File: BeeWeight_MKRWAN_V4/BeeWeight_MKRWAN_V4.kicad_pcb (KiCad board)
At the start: 2 copper layers, 38.2 x 67.4 mm, 31 parts, among them J10 694103107102, J2 691412120004B, J3 691412120004B, J4 691412120004B, J5 691412120004B, J7 Conn_01x14_Female, J8 Conn_01x14_Female, J9 694108301002, Q1 IRLML6244, U1 ADS1241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

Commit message: Lundi soir : en cours de pin mapping
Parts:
- added J1: SSW-120-01-X-S, SAMTEC_SSW-120-01-X-S, F.Cu at (153.6, 81.7)
- added J6: SSW-120-01-X-S, SSW-120-01-X-S:SAMTEC_SSW-120-01-X-S, F.Cu at (244.9, 84.2)
- added U3: LDL1117S33R, SOT230P700X180-4N, F.Cu at (206.4, 61.7)
- moved J7 86.4 mm to (67.5, 65.6)
- moved J8 86.4 mm to (87.8, 98.6)
- moved J9 32.5 mm to (163.6, 25.7)
- moved J10 30.8 mm to (145.3, 29.2)
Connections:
- net Net-(U2-Pad3) renamed /IO42_ALERT
- net Net-(U2-Pad6) renamed /IO42_SHT_RST
- Q1 pad 1: /D3_CMD_MOS -> /IO42_CMD_MOS
- R1 pad 2: /D3_CMD_MOS -> /IO42_CMD_MOS
- R6 pad 1: /D12_SCL -> /IO42_SCL
- R7 pad 1: /D11_SDA -> /IO42_SDA
- U1 pad 23: /D7_CS -> /IO42_CS
- U1 pad 24: /D8_MOSI -> /IO42_MOSI
- U1 pad 25: /D10_MISO -> /IO42_MISO
- U1 pad 26: /D9_SCLK -> /IO42_SCLK
- U2 pad 1: /D11_SDA -> /IO42_SDA
- U2 pad 4: /D12_SCL -> /IO42_SCL
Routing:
- net /IO42_SCL: track 0.00 -> 44.0 mm, vias 0 -> 1
- net /D12_SCL: track 44.0 -> 0.00 mm, vias 1 -> 0
- net /IO42_SDA: track 0.00 -> 38.1 mm, vias 0 -> 2
- net /D11_SDA: track 38.1 -> 0.00 mm, vias 2 -> 0
- net /IO42_CMD_MOS: track 0.00 -> 15.7 mm
- net /D3_CMD_MOS: track 15.7 -> 0.00 mm
- net /IO42_CS: track 0.00 -> 14.4 mm
- net /D7_CS: track 14.4 -> 0.00 mm
- net /IO42_MOSI: track 0.00 -> 13.9 mm
- net /D8_MOSI: track 13.9 -> 0.00 mm
- net /IO42_SCLK: track 0.00 -> 11.2 mm
- net /D9_SCLK: track 11.2 -> 0.00 mm
- net /IO42_MISO: track 0.00 -> 10.6 mm, vias 0 -> 1
- net /D10_MISO: track 10.6 -> 0.00 mm, vias 1 -> 0
- net /Vin: track 27.1 -> 18.8 mm
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
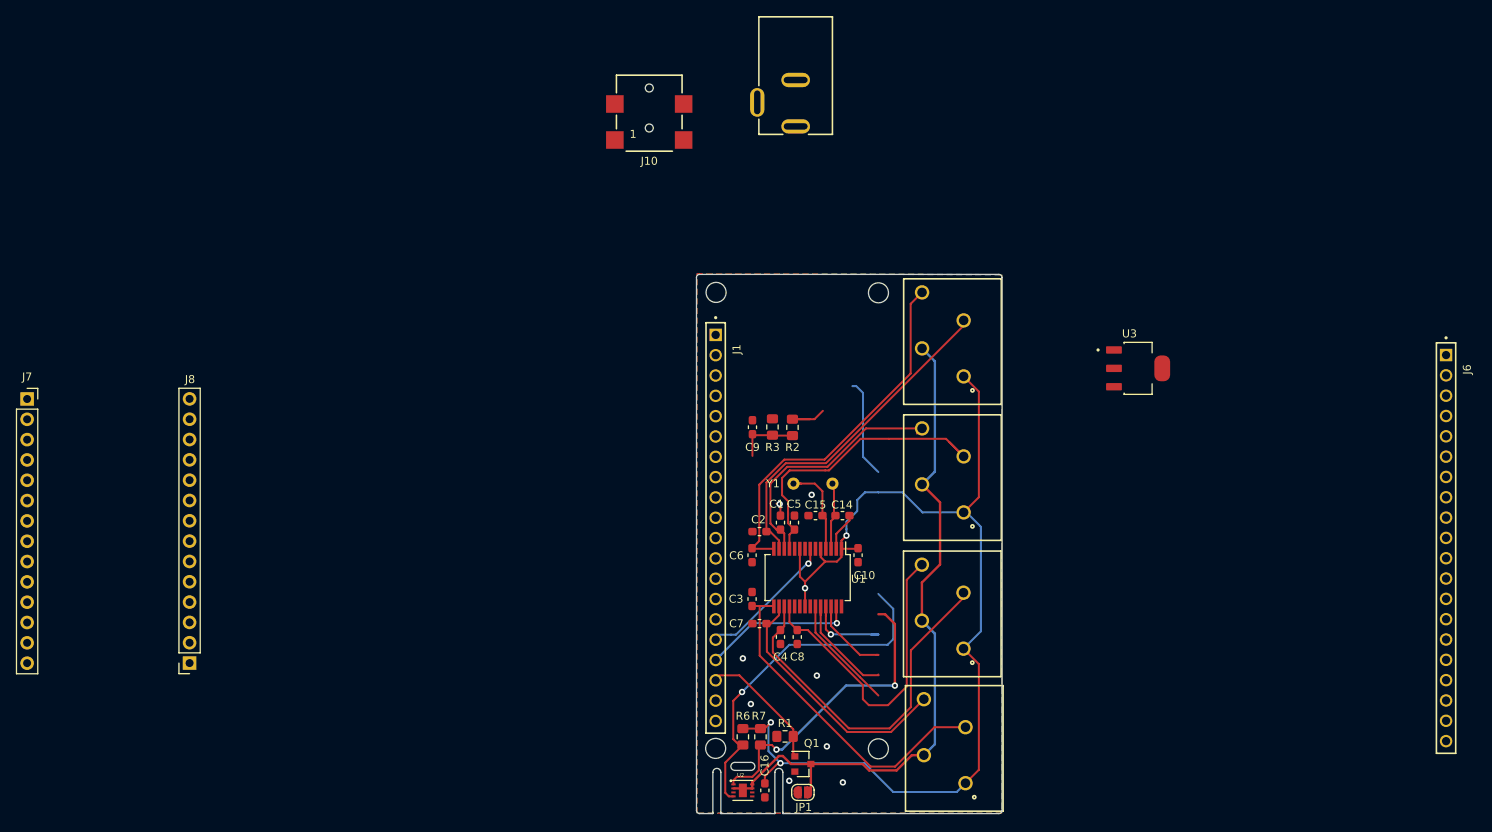
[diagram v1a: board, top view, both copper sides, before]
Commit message: Mardi soir: pinout routé sur le schematic
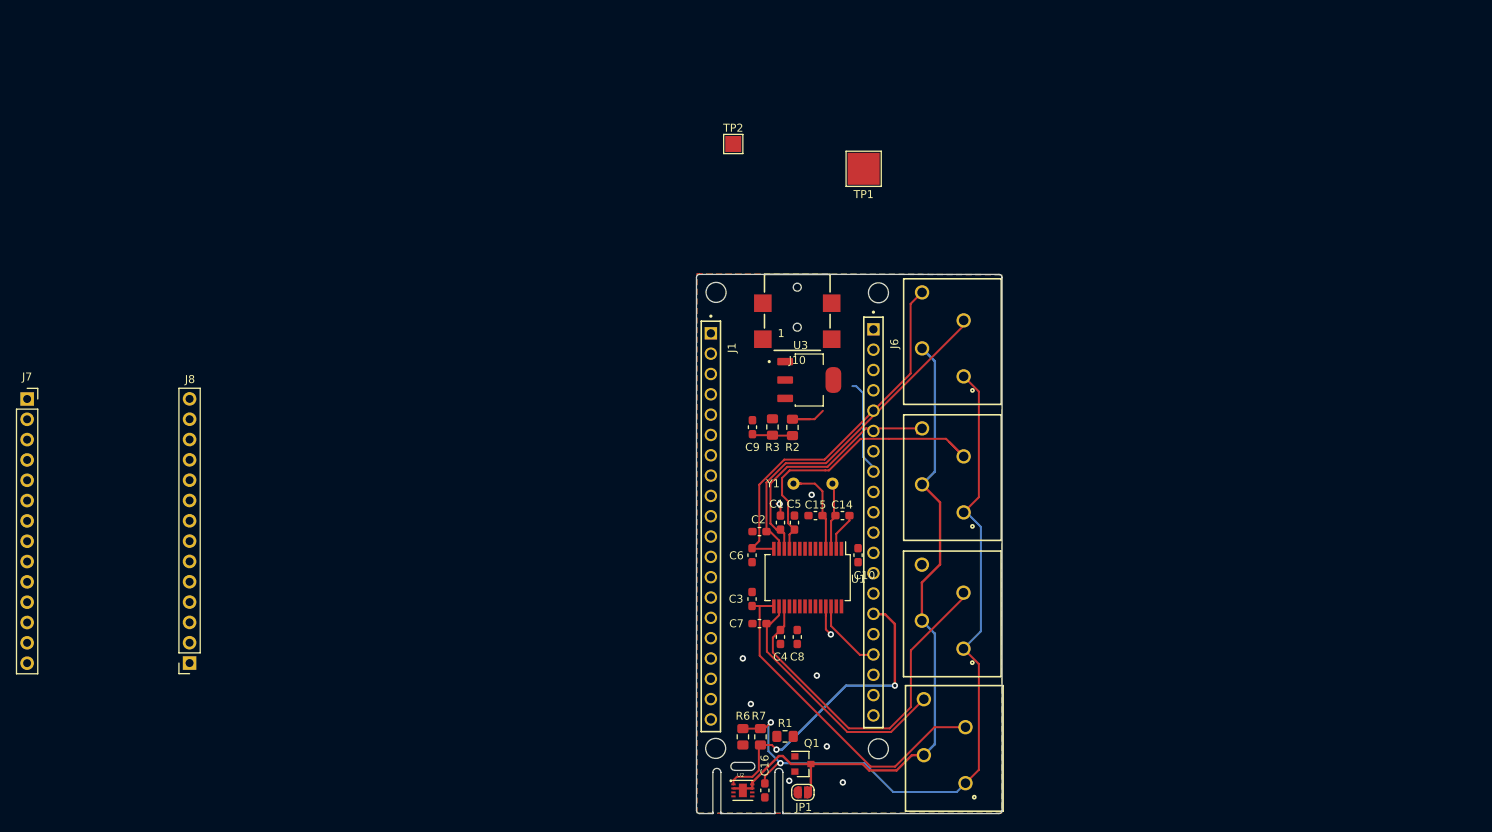
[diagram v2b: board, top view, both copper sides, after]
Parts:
- removed J9: 694108301002, USMB_Syl_Mont:Jack_DC_2.1mm Wurth_694108301002
- added TP1: TestPoint, TestPoint:TestPoint_Pad_4.0x4.0mm, F.Cu at (172.1, 36.8)
- added TP2: TestPoint, TestPoint:TestPoint_Pad_2.0x2.0mm, F.Cu at (155.8, 33.7)
- U3: value LDL1117S33R -> LDL1117S50R
- moved J6 71.7 mm to (173.3, 81.0)
- moved U3 41.1 mm to (165.3, 63.2)
- moved J10 31.0 mm to (163.8, 54.1)
- moved J1 0.63 mm to (153.0, 81.5)
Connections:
- C9 pad 1: /A1_D16_Vin -> /IO4_VBAT_12V
- J1 pad 03: Net-(J1-Pad03) -> GND
- J1 pad 07: Net-(J1-Pad07) -> /IO34_CS
- J1 pad 08: Net-(J1-Pad08) -> /IO35_MOSI
- J1 pad 09: Net-(J1-Pad09) -> /IO36_SCLK
- J1 pad 10: Net-(J1-Pad10) -> /IO37_MISO
- J1 pad 11: Net-(J1-Pad11) -> /IO38_PDWN
- J1 pad 12: Net-(J1-Pad12) -> /IO39_DRDY
- J10 pad 1: Net-(J10-Pad1) -> /12V
- J10 pad 2: Net-(J10-Pad2) -> GND
- J10 pad A1: Net-(J10-Pad1) -> /12V
- J6 pad 01: Net-(J6-Pad01) -> /VDD_5V
- J6 pad 02: Net-(J6-Pad02) -> /3V3
- J6 pad 03: Net-(J6-Pad03) -> GND
- J6 pad 09: Net-(J6-Pad09) -> /IO18_SCL
- J6 pad 10: Net-(J6-Pad10) -> /IO21_SHT_RST
- J6 pad 11: Net-(J6-Pad11) -> /IO19_SHT_ALERT
- J6 pad 12: Net-(J6-Pad12) -> /IO17_SDA
- J6 pad 17: Net-(J6-Pad17) -> /IO7_CMD_MOS
- J6 pad 20: Net-(J6-Pad20) -> /IO4_VBAT_12V
- Q1 pad 1: /IO42_CMD_MOS -> /IO7_CMD_MOS
- R1 pad 2: /IO42_CMD_MOS -> /IO7_CMD_MOS
- R2 pad 1: /A1_D16_Vin -> /IO4_VBAT_12V
- R2 pad 2: /Vin -> /12V
- R3 pad 2: /A1_D16_Vin -> /IO4_VBAT_12V
- R6 pad 1: /IO42_SCL -> /IO18_SCL
- R7 pad 1: /IO42_SDA -> /IO17_SDA
- U1 pad 23: /IO42_CS -> /IO34_CS
- U1 pad 24: /IO42_MOSI -> /IO35_MOSI
- U1 pad 25: /IO42_MISO -> /IO37_MISO
- U1 pad 26: /IO42_SCLK -> /IO36_SCLK
- U1 pad 27: /D2_DRDY -> /IO39_DRDY
- U1 pad 7: /D1_PDWN -> /IO38_PDWN
- U2 pad 1: /IO42_SDA -> /IO17_SDA
- U2 pad 3: /IO42_ALERT -> /IO19_SHT_ALERT
- U2 pad 4: /IO42_SCL -> /IO18_SCL
- U2 pad 6: /IO42_SHT_RST -> /IO21_SHT_RST
- U3 pad 1: Net-(U3-Pad1) -> GND
- U3 pad 2: Net-(U3-Pad2) -> /VDD_5V
- U3 pad 3: Net-(U3-Pad3) -> /12V
- U3 pad 4: Net-(U3-Pad2) -> /VDD_5V
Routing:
- net /IO42_SCL: track 44.0 -> 0.00 mm, vias 1 -> 0
- net /3V3: track 134.1 -> 94.2 mm, vias 4 -> 2
- net /AIN3: track 38.9 -> 0.00 mm
- net /D2_DRDY: track 18.9 -> 0.00 mm, vias 1 -> 0
- net /Vin: track 18.8 -> 0.00 mm
- net /D1_PDWN: track 17.2 -> 0.00 mm, vias 1 -> 0
- net /IO42_CMD_MOS: track 15.7 -> 0.00 mm
- net /IO42_CS: track 14.4 -> 0.00 mm
- net /IO42_MOSI: track 13.9 -> 0.00 mm
- net Net-(J6-Pad08): track 0.00 -> 12.4 mm
- net /IO42_MISO: track 10.6 -> 0.00 mm, vias 1 -> 0
- net /A1_D16_Vin: track 7.78 -> 0.00 mm
- net /12V: track 0.00 -> 6.48 mm
- net /IO4_VBAT_12V: track 0.00 -> 5.07 mm
- net /IO37_MISO: track 0.00 -> 3.76 mm, vias 0 -> 1
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
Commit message: Tout mis au propre (chemin + pistes et positions)
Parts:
- TP2: footprint TestPoint:TestPoint_Pad_2.0x2.0mm -> TestPoint:TestPoint_Pad_4.0x4.0mm
- moved TP2 19.3 mm to (155.0, 53.0)
- moved TP1 16.2 mm to (173.0, 53.0)
- moved J6 2.00 mm to (173.3, 83.0)
- moved J1 1.50 mm to (153.0, 83.0)
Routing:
- net /3V3: track 94.2 -> 0.00 mm, vias 2 -> 0
- net /GND_LowPower: track 87.3 -> 0.00 mm
- net /AIN5: track 46.5 -> 0.00 mm
- net /AIN2: track 45.7 -> 0.00 mm
- net /AIN4: track 42.6 -> 0.00 mm
- net /AIN6: track 42.5 -> 0.00 mm
- net /AIN0: track 38.3 -> 0.00 mm
- net /IO42_SDA: track 38.1 -> 0.00 mm, vias 2 -> 0
- net /AIN7: track 32.1 -> 0.00 mm
- net /AIN1: track 31.9 -> 0.00 mm
- net Net-(J6-Pad08): track 12.4 -> 0.00 mm
- net Net-(C15-Pad1): track 12.1 -> 0.00 mm
- net /IO42_SCLK: track 11.2 -> 0.00 mm
- net Net-(C14-Pad2): track 9.08 -> 0.00 mm
- net GND: track 6.54 -> 0.00 mm, vias 8 -> 0
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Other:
- board size 38.2 x 67.4 mm -> 51 x 71.7 mm

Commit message: FINISHED
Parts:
- removed J7, J8: Conn_01x14_Female, Connector_PinSocket_2.54mm:PinSocket_1x14_P2.54mm_Vertical
- removed TP2: TestPoint, TestPoint:TestPoint_Pad_4.0x4.0mm
- added 12V: TestPoint, TestPoint:TestPoint_Pad_4.0x4.0mm, F.Cu at (155.0, 53.0)
- moved C9 1.50 mm to (158.2, 70.6)
- moved R2 1.50 mm to (163.2, 70.6)
- moved R3 1.50 mm to (160.7, 70.6)
- moved U3 1.30 mm to (165.3, 64.5)
- moved J10 0.90 mm to (163.8, 55.0)
- moved C10 0.20 mm to (171.2, 85.1)
- renumbered TP1 to GND
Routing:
- net /3V3: track 0.00 -> 144.1 mm, vias 0 -> 2
- net /GND_LowPower: track 0.00 -> 87.3 mm
- net /IO4_VBAT_12V: track 0.00 -> 47.6 mm, vias 0 -> 1
- net /IO18_SCL: track 0.00 -> 45.7 mm
- net /AIN5: track 0.00 -> 44.0 mm
- net /AIN4: track 0.00 -> 41.3 mm
- net /IO21_SHT_RST: track 0.00 -> 40.5 mm
- net /IO19_SHT_ALERT: track 0.00 -> 39.3 mm
- net /AIN6: track 0.00 -> 36.1 mm, vias 0 -> 1
- net /IO17_SDA: track 0.00 -> 35.3 mm
- net /AIN0: track 0.00 -> 32.7 mm
- net /AIN1: track 0.00 -> 29.6 mm
- net /AIN2: track 0.00 -> 28.4 mm, vias 0 -> 1
- net /AIN7: track 0.00 -> 25.6 mm, vias 0 -> 1
- net /IO35_MOSI: track 0.00 -> 24.1 mm, vias 0 -> 1
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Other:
- board size 51 x 71.7 mm -> 38.2 x 67.4 mm
- copper layers 2 -> 4
- net class Default: clearance 0.2 -> 0.127; trace_width 0.25 -> 0.127; via_dia 0.8 -> 0.6; via_drill 0.4 -> 0.3
- net class Power removed
- rule pad_to_mask_clearance: 0.051 -> 0
- rule solder_mask_min_width: 0.25 -> 0.12
- rule trace_clearance: 0.2 -> 0.127
- rule trace_min: 0.2 -> 0.127
- rule via_min_size: 0.4 -> 0.6
- board text added: "+"
- board text added: "-"
- board text added: "Bee Weight WS Lite V3 USMB-ADTP Version 4"
- board text removed: "Battery 3.7V"
- board text removed: "Bee Weight MKRWAN USMB Version 4"
- board text removed: "Solar Panel or 4V-17V DC"

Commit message: Send to JLCPCB
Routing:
- net GND: vias 49 -> 51
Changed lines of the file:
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@@
     (thickness 1.6002)
     (drawings 51)
-    (tracks 331)
+    (tracks 333)
     (zones 0)
     (modules 33)
@@
   )
   (setup
-    (last_trace_width 0.6)
+    (last_trace_width 0.127)
     (user_trace_width 0.15)
     (user_trace_width 0.2)
@@
     (effects (font (size 0.8 0.8) (thickness 0.15)) (justify mirror))
   )
-  (gr_text "Bee Weight WS Lite V3\nUSMB-ADTP\nVersion 4" (at 169.5 112) (layer B.SilkS)
+  (gr_text "Bee Weight WS Lite V3\nUSMB-ADTP\nVersion 4" (at 163 103) (layer B.SilkS)
     (effects (font (size 1 1) (thickness 0.15)) (justify mirror))
   )
+  (via (at 157 66) (size 3.5) (drill 3.1) (layers Front Back) (net 1))
   (segment (start 172.4 53.6) (end 173 53) (width 0.3) (layer Front) (net 1))
   (via (at 175.5 64) (size 0.6) (layers Front Back) (net 1))
@@
   (via (at 183 108) (size 0.6) (drill 0.3) (layers Front Back) (net 1))
   (via (at 183.5 116) (size 0.6) (drill 0.3) (layers Front Back) (net 1))
-  (via (at 172.5 116) (size 0.6) (drill 0.3) (layers Front Back) (net 1))
   (via (at 152.5 116) (size 0.6) (drill 0.3) (layers Front Back) (net 1))
   (via (at 155 116) (size 0.6) (drill 0.3) (layers Front Back) (net 1))
@@
   (via (at 157 98) (size 0.6) (drill 0.3) (layers Front Back) (net 1))
   (via (at 157 102.5) (size 0.6) (drill 0.3) (layers Front Back) (net 1))
-  (via (at 157 67) (size 0.6) (drill 0.3) (layers Front Back) (net 1))
   (via (at 157 63) (size 0.6) (drill 0.3) (layers Front Back) (net 1))
   (via (at 157 59) (size 0.6) (drill 0.3) (layers Front Back) (net 1))
@@
   (via (at 161.75 78.5) (size 0.6) (drill 0.3) (layers Front Back) (net 1))
   (via (at 169 89.5) (size 0.6) (drill 0.3) (layers Front Back) (net 1))
+  (via (at 173 115) (size 3.5) (drill 3.1) (layers Front Back) (net 1))
+  (via (at 170 95) (size 0.6) (drill 0.3) (layers Front Back) (net 1))
+  (via (at 163 101) (size 0.6) (drill 0.3) (layers Front Back) (net 1))
   (segment (start 162.175 84.3) (end 162.175 82.375) (width 0.127) (layer Front) (net 2))
   (segment (start 162.175 82.375) (end 161.7 81.9) (width 0.127) (layer Front) (net 2))
